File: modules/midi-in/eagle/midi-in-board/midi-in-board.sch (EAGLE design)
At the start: 75 parts, among them IC1 LM358N, IC2 TL072P, IC3 TL074P, IC4 TL074P, T1 BC547, T2 BC547, X1 POWER IN, X2 MIDI IN, X3 MIDI THRU, X4 CHANNEL SELECT SW

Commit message: Progress on MIDI in main board. Nightmare.
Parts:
- removed JP1: (no value), pinhead:PINHD-1X55X2MM
- added X5: 22-23-2051, con-molex:22-23-2051
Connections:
- removed net GND: C1.2, C2.2, C3.2, C4.2, C5.2, C6.2, IC1P.V-, IC2B.+IN, IC3B.+IN, IC3D.+IN, IC4B.+IN, IC4D.+IN, JP1.1, JP2.2, JP3.2, OK1.GND, R10.2, R11.2, R12.2, R14.1, R16.1, R28.1, R8.2, R9.2, SV1.2, X1-2.KL, X3-2.S, X4-2.S
- removed net N$43: IC4P.V-
- new net N$8: C1.2, C2.2, C3.2, C4.2, C5.2, C6.2, IC1P.V-, IC2B.+IN, IC3B.+IN, IC3D.+IN, IC4B.+IN, IC4D.+IN, JP2.2, JP3.2, OK1.GND, R10.2, R11.2, R12.2, R14.1, R16.1, R28.1, R8.2, R9.2, SV1.2, X1-2.KL, X3-2.S, X4-2.S, X5-1.S
- net N$24: now also X5-4.S; no longer JP1.4
- net N$26: now also X5-3.S; no longer JP1.3
- net N$41: now also IC4P.V-
- net N$9: now also X5-5.S; no longer JP1.5
- net VCC: now also X5-2.S; no longer JP1.2
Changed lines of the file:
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@@
 <?xml version="1.0" encoding="utf-8"?>
 <!DOCTYPE eagle SYSTEM "eagle.dtd">
-<eagle version="7.5.0">
+<eagle version="7.3.0">
 <drawing>
 <settings>
@@
 <part name="JP3" library="pinhead" deviceset="PINHD-1X2" device=""/>
 <part name="SUPPLY17" library="supply2" deviceset="GND" device=""/>
-<part name="JP1" library="pinhead" deviceset="PINHD-1X5" device="5X2MM"/>
 <part name="SUPPLY10" library="supply2" deviceset="GND" device=""/>
 <part name="P+8" library="supply1" deviceset="VCC" device=""/>
+<part name="X5" library="con-molex" deviceset="22-23-2051" device=""/>
 </parts>
 <sheets>
@@
 <text x="7.62" y="69.85" size="1.778" layer="91">DIN5 CASE</text>
 <text x="135.636" y="135.382" size="1.778" layer="91">Arduino pro micro</text>
-<text x="144.78" y="195.58" size="1.778" layer="91" rot="R90">LATCH</text>
-<text x="139.7" y="195.58" size="1.778" layer="91" rot="R90">DATA OUT</text>
+<text x="144.78" y="203.2" size="1.778" layer="91" rot="R90">LATCH</text>
+<text x="139.7" y="203.2" size="1.778" layer="91" rot="R90">DATA OUT</text>
 <text x="172.72" y="101.6" size="1.778" layer="91">PIN_FREQ</text>
 <text x="172.72" y="114.3" size="1.778" layer="91">PIN_TRIGGER</text>
 <text x="172.72" y="109.22" size="1.778" layer="91">PIN_GATE</text>
-<text x="142.24" y="195.58" size="1.778" layer="91" rot="R90">CLK</text>
+<text x="142.24" y="203.2" size="1.778" layer="91" rot="R90">CLK</text>
 <text x="96.52" y="45.72" size="1.778" layer="91">PIN_CHANNEL_SELECT_BUTTON</text>
 <text x="172.72" y="81.28" size="1.778" layer="91">PIN_MOD1</text>
@@
 <text x="368.3" y="149.86" size="1.778" layer="91">GATE
 LED</text>
-<text x="147.32" y="195.58" size="1.778" layer="91" rot="R90">VCC</text>
-<text x="149.86" y="195.58" size="1.778" layer="91" rot="R90">GND</text>
+<text x="147.32" y="203.2" size="1.778" layer="91" rot="R90">VCC</text>
+<text x="149.86" y="203.2" size="1.778" layer="91" rot="R90">GND</text>
 </plain>
 <instances>
@@
 <instance part="JP3" gate="G$1" x="365.76" y="149.86"/>
 <instance part="SUPPLY17" gate="GND" x="355.6" y="144.78"/>
-<instance part="JP1" gate="A" x="144.78" y="193.04" rot="MR90"/>
 <instance part="SUPPLY10" gate="GND" x="149.86" y="180.34"/>
 <instance part="P+8" gate="VCC" x="157.48" y="198.12"/>
+<instance part="X5" gate="-1" x="149.86" y="193.04" rot="MR90"/>
+<instance part="X5" gate="-2" x="147.32" y="193.04" rot="MR90"/>
+<instance part="X5" gate="-3" x="144.78" y="193.04" rot="MR90"/>
+<instance part="X5" gate="-4" x="142.24" y="193.04" rot="MR90"/>
+<instance part="X5" gate="-5" x="139.7" y="193.04" rot="MR90"/>
 </instances>
 <busses>
@@
 </segment>
 </net>
-<net name="GND" class="0">
+<net name="N$8" class="0">
 <segment>
 <pinref part="OK1" gate="A" pin="GND"/>
@@
 </segment>
 <segment>
-<pinref part="JP1" gate="A" pin="1"/>
 <pinref part="SUPPLY10" gate="GND" pin="GND"/>
 <wire x1="149.86" y1="190.5" x2="149.86" y2="182.88" width="0.1524" layer="91"/>
+<pinref part="X5" gate="-1" pin="S"/>
 </segment>
 </net>
@@
 <wire x1="139.7" y1="160.02" x2="152.4" y2="160.02" width="0.1524" layer="91"/>
 <wire x1="152.4" y1="160.02" x2="152.4" y2="147.32" width="0.1524" layer="91"/>
-<pinref part="JP1" gate="A" pin="5"/>
 <wire x1="139.7" y1="190.5" x2="139.7" y2="160.02" width="0.1524" layer="91"/>
+<pinref part="X5" gate="-5" pin="S"/>
 </segment>
 </net>
@@
 <wire x1="149.86" y1="119.38" x2="172.72" y2="119.38" width="0.1524" layer="91"/>
 <wire x1="172.72" y1="119.38" x2="172.72" y2="162.56" width="0.1524" layer="91"/>
-<pinref part="JP1" gate="A" pin="4"/>
 <wire x1="142.24" y1="190.5" x2="142.24" y2="162.56" width="0.1524" layer="91"/>
 <wire x1="142.24" y1="162.56" x2="172.72" y2="162.56" width="0.1524" layer="91"/>
+<pinref part="X5" gate="-4" pin="S"/>
 </segment>
 </net>
@@
 <wire x1="149.86" y1="147.32" x2="149.86" y2="154.94" width="0.1524" layer="91"/>
 <wire x1="149.86" y1="154.94" x2="144.78" y2="154.94" width="0.1524" layer="91"/>
-<pinref part="JP1" gate="A" pin="3"/>
 <wire x1="144.78" y1="154.94" x2="144.78" y2="190.5" width="0.1524" layer="91"/>
+<pinref part="X5" gate="-3" pin="S"/>
 </segment>
 </net>
@@
 <wire x1="45.72" y1="165.1" x2="53.34" y2="165.1" width="0.1524" layer="91"/>
 <junction x="53.34" y="165.1"/>
-</segment>
-</net>
-<net name="N$43" class="0">
-<segment>
 <pinref part="IC4" gate="P" pin="V-"/>
-<wire x1="68.58" y1="167.64" x2="68.58" y2="165.1" width="0.1524" layer="91"/>
+<wire x1="68.58" y1="165.1" x2="68.58" y2="167.64" width="0.1524" layer="91"/>
 </segment>
 </net>
@@
 </segment>
 <segment>
-<pinref part="JP1" gate="A" pin="2"/>
 <wire x1="147.32" y1="190.5" x2="147.32" y2="185.42" width="0.1524" layer="91"/>
 <wire x1="147.32" y1="185.42" x2="157.48" y2="185.42" width="0.1524" layer="91"/>
 <pinref part="P+8" gate="VCC" pin="VCC"/>
 <wire x1="157.48" y1="185.42" x2="157.48" y2="195.58" width="0.1524" layer="91"/>
-</segment>
-<segment>
+<pinref part="X5" gate="-2" pin="S"/>
+</segment>
+<segment>

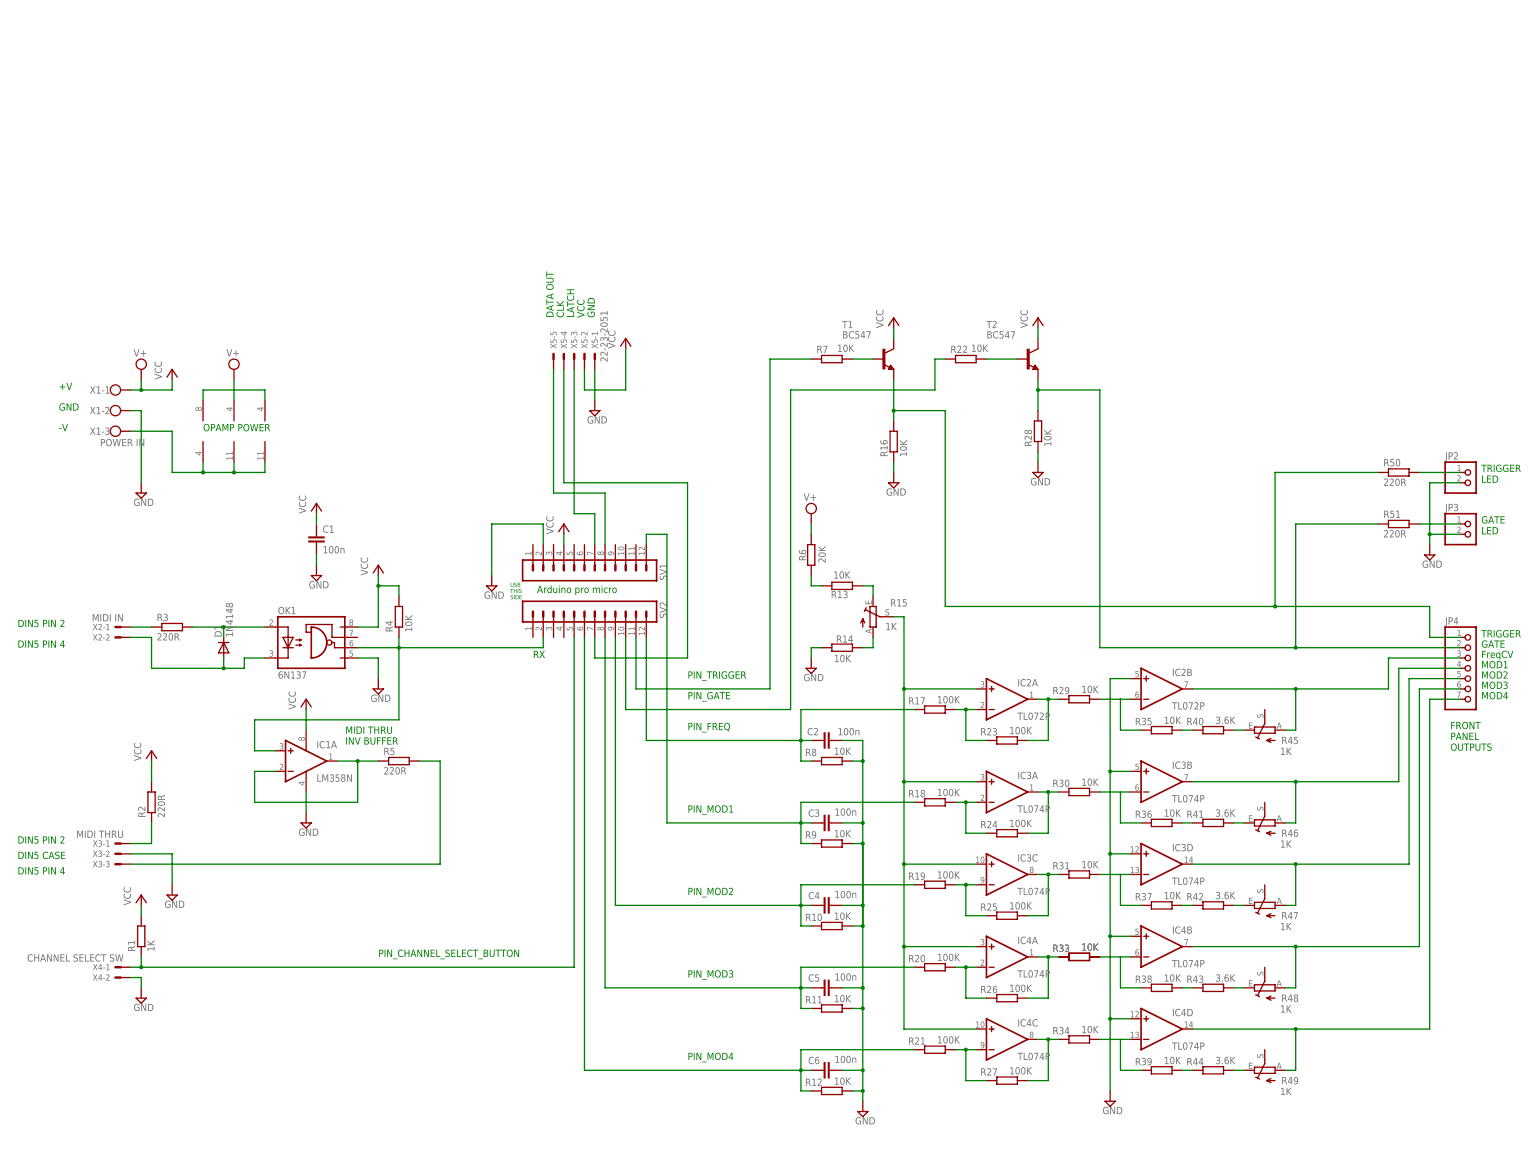
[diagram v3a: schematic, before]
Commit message: Separate out CV scaling to its own board, finish MIDI in board layout
Non-nightmare!
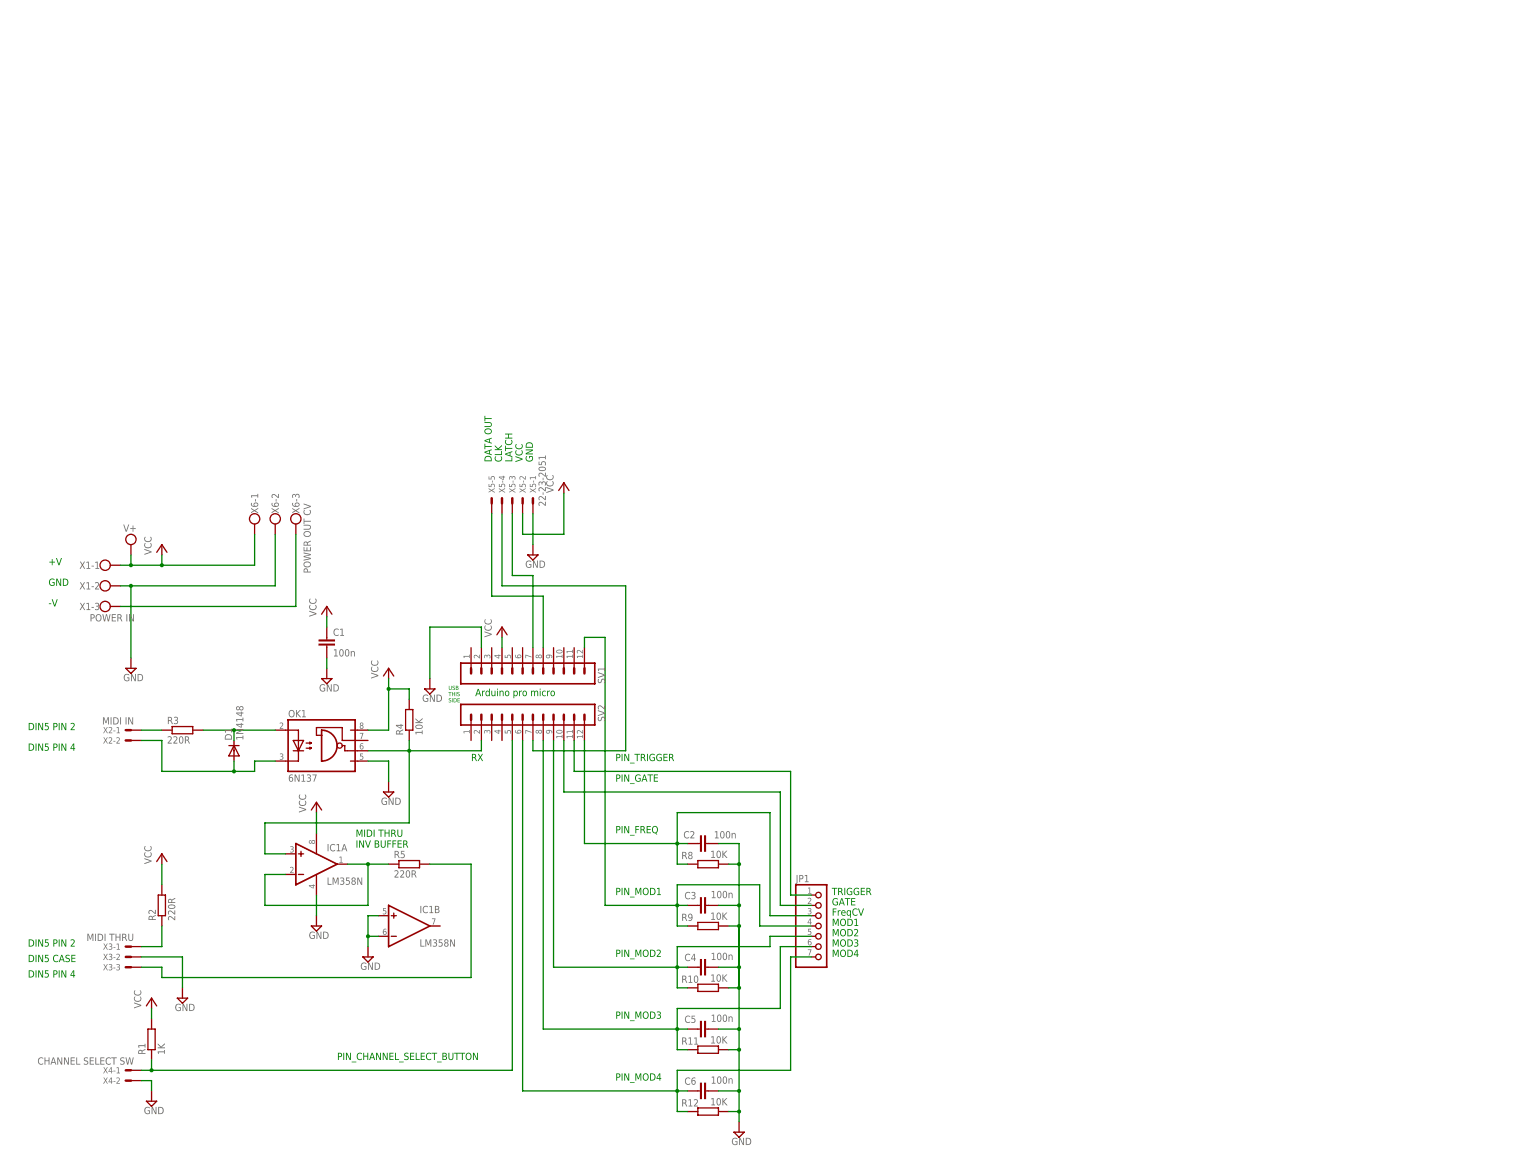
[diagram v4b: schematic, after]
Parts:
- removed IC2: TL072P, linear:TL072P
- removed IC3, IC4: TL074P, linear:TL074P
- removed JP2, JP3: (no value), pinhead:PINHD-1X2
- removed JP4: (no value), pinhead:PINHD-1X7
- removed R13, R14, R16, R22, R28, R29, R30, R31, R32, R33, R34, R35, R36, R37, R38, R39, R7: 10K, rcl:R-EU_0207/7
- removed R15, R45, R46, R47, R48, R49: 1K, pot:TRIM_EU-CA6V
- removed R17, R18, R19, R20, R21, R23, R24, R25, R26, R27: 100K, rcl:R-EU_0207/7
- removed R40, R41, R42, R43, R44: 3.6K, rcl:R-EU_0207/7
- removed R50, R51: 220R, rcl:R-EU_0207/7
- removed R6: 20K, rcl:R-EU_0207/7
- removed T1, T2: BC547, transistor:BC547
- added JP1: (no value), pinhead:PINHD-1X7
- added X6: POWER OUT CV, con-wago-500:W237-103
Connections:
- removed net N$15: C3.1, R18.1, R9.1, SV1.12
- removed net N$19: R7.2, T1.B
- removed net N$21: R22.2, T2.B
- removed net N$22: JP4.2, R28.2, R51.1, T2.E
- removed net N$23: IC4A.OUT, R26.2, R32.1, R33.1
- removed net N$27: IC2A.-IN, R17.2, R23.1
- removed net N$28: IC3A.-IN, R18.2, R24.1
- removed net N$29: IC3C.-IN, R19.2, R25.1
- removed net N$31: IC4A.-IN, R20.2, R26.1
- removed net N$32: IC4C.-IN, R21.2, R27.1
- removed net N$33: IC2A.OUT, R23.2, R29.1
- removed net N$34: IC2B.-IN, R29.2, R35.1
- removed net N$35: IC3A.OUT, R24.2, R30.1
- removed net N$36: IC3B.-IN, R30.2, R36.1
- removed net N$37: IC3C.OUT, R25.2, R31.1
- removed net N$38: IC3D.-IN, R31.2, R37.1
- removed net N$39: IC4C.OUT, R27.2, R34.1
- removed net N$40: IC4D.-IN, R34.2, R39.1
- removed net N$41: IC2P.V-, IC3P.V-, IC4P.V-, X1-3.KL
- removed net N$42: R14.2, R15.A
- removed net N$44: R13.2, R6.1
- removed net N$45: R13.1, R15.E
- removed net N$46: IC2A.+IN, IC3A.+IN, IC3C.+IN, IC4A.+IN, IC4C.+IN, R15.S
- removed net N$53: R35.2, R40.1
- removed net N$56: R36.2, R41.1
- removed net N$57: R37.2, R42.1
- removed net N$59: R38.2, R43.1
- removed net N$61: R39.2, R44.1
- removed net N$62: R40.2, R45.E
- removed net N$63: R41.2, R46.E
- removed net N$64: R42.2, R47.E
- removed net N$65: R43.2, R48.E
- removed net N$66: R44.2, R49.E
- removed net N$67: IC2B.OUT, JP4.3, R45.A
- removed net N$68: IC3B.OUT, JP4.4, R46.A
- removed net N$69: IC3D.OUT, JP4.5, R47.A
- removed net N$70: IC4B.OUT, JP4.6, R48.A
- removed net N$71: IC4D.OUT, JP4.7, R49.A
- removed net N$79: JP2.1, R50.2
- removed net N$8: C1.2, C2.2, C3.2, C4.2, C5.2, C6.2, IC1P.V-, IC2B.+IN, IC3B.+IN, IC3D.+IN, IC4B.+IN, IC4D.+IN, JP2.2, JP3.2, OK1.GND, R10.2, R11.2, R12.2, R14.1, R16.1, R28.1, R8.2, R9.2, SV1.2, X1-2.KL, X3-2.S, X4-2.S, X5-1.S
- removed net N$80: JP3.1, R51.2
- new net GND: C1.2, C2.2, C3.2, C4.2, C5.2, C6.2, IC1B.+IN, IC1B.-IN, IC1P.V-, OK1.GND, R10.2, R11.2, R12.2, R8.2, R9.2, SV1.2, X1-2.KL, X3-2.S, X4-2.S, X5-1.S, X6-2.KL
- net N$10: now also X1-3.KL, X6-3.KL; no longer IC4B.-IN, R32.2, R33.2, R38.1
- net N$11: now also JP1.1; no longer R7.1
- net N$12: now also JP1.2; no longer R22.1
- net N$13: now also JP1.3; no longer R17.1
- net N$16: now also JP1.5; no longer R19.1
- net N$17: now also JP1.6; no longer R20.1
- net N$18: now also JP1.7; no longer R21.1
- net N$20: now also C3.1, JP1.4, R9.1, SV1.12; no longer JP4.1, R16.2, R50.1, T1.E
- net VCC: now also X6-1.KL; no longer IC2P.V+, IC3P.V+, IC4P.V+, R6.2, T1.C, T2.C
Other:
- note removed: "FRONT PANEL OUTPUTS"
- note removed: "GATE LED"
- note removed: "OPAMP POWER"
- note removed: "TRIGGER LED"
- moved on the sheet: C1, C2, C3, C4, C5, C6, D1, IC1A, OK1, R1, R10, R11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
